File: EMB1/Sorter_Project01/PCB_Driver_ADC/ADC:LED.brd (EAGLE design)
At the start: 100 x 80 mm, 17 parts, among them IC2 LM358N, K1 612006235121, Q1 IRF512, Q2 IRF512, Q3 IRF512, Q4 IRF512

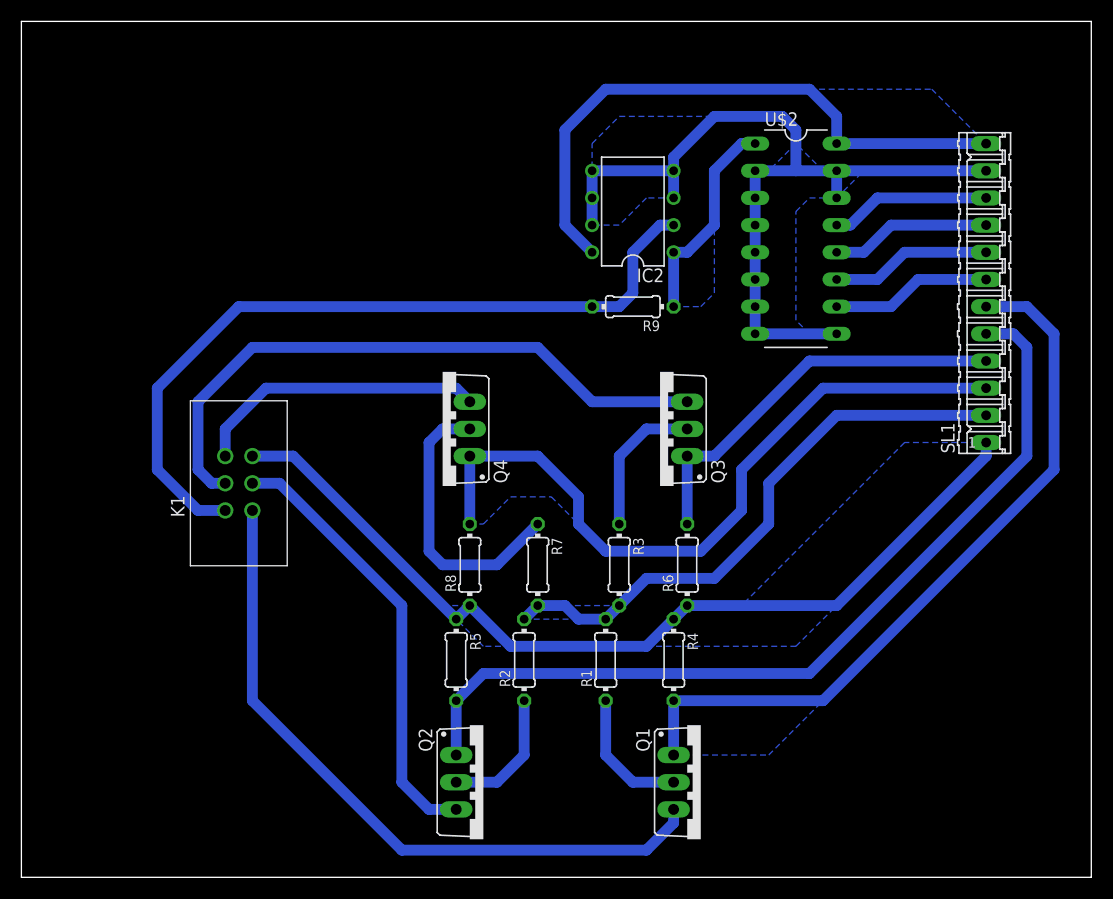
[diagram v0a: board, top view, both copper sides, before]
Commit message: Driver/ADC board modified
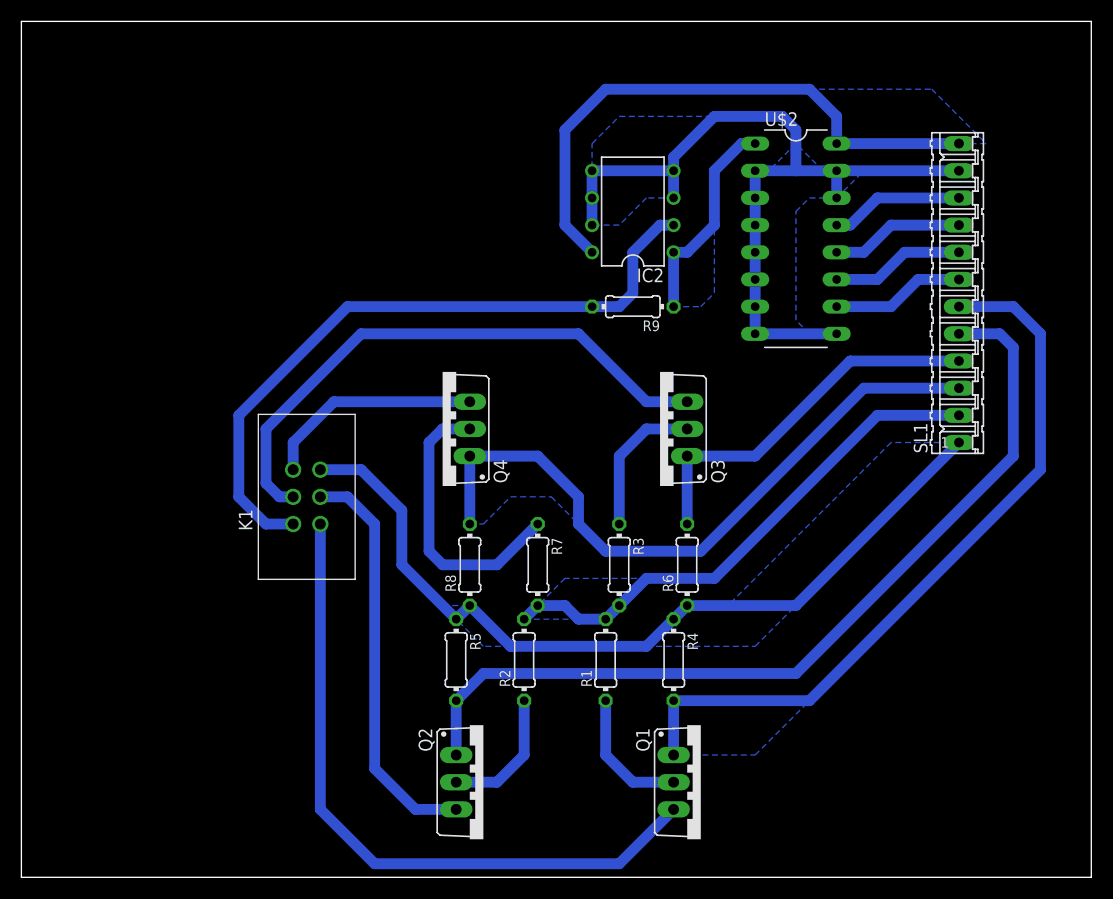
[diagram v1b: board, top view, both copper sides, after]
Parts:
- moved K1 6.48 mm to (26.7, 35.6)
- moved SL1 2.54 mm to (87.6, 54.6)
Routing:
- net GND: track 166.5 -> 156.8 mm
- net PHD: track 72.4 -> 64.0 mm
- net LED4: track 27.5 -> 20.6 mm
- net LED3: track 59.3 -> 53.8 mm
- net CTRL4: track 68.3 -> 63.6 mm
- net 12V: track 54.4 -> 49.6 mm
- net LED2: track 41.3 -> 38.2 mm
- net VDD: track 57.0 -> 54.5 mm
- net DOUT: track 15.0 -> 12.5 mm
- net DIN: track 15.0 -> 12.5 mm
- net CTRL3: track 38.0 -> 35.4 mm
- net CLK: track 15.0 -> 12.5 mm
- net *CS: track 15.0 -> 12.5 mm
- net LED1: track 65.3 -> 63.9 mm

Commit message: Printed schematic ADC/LEDS
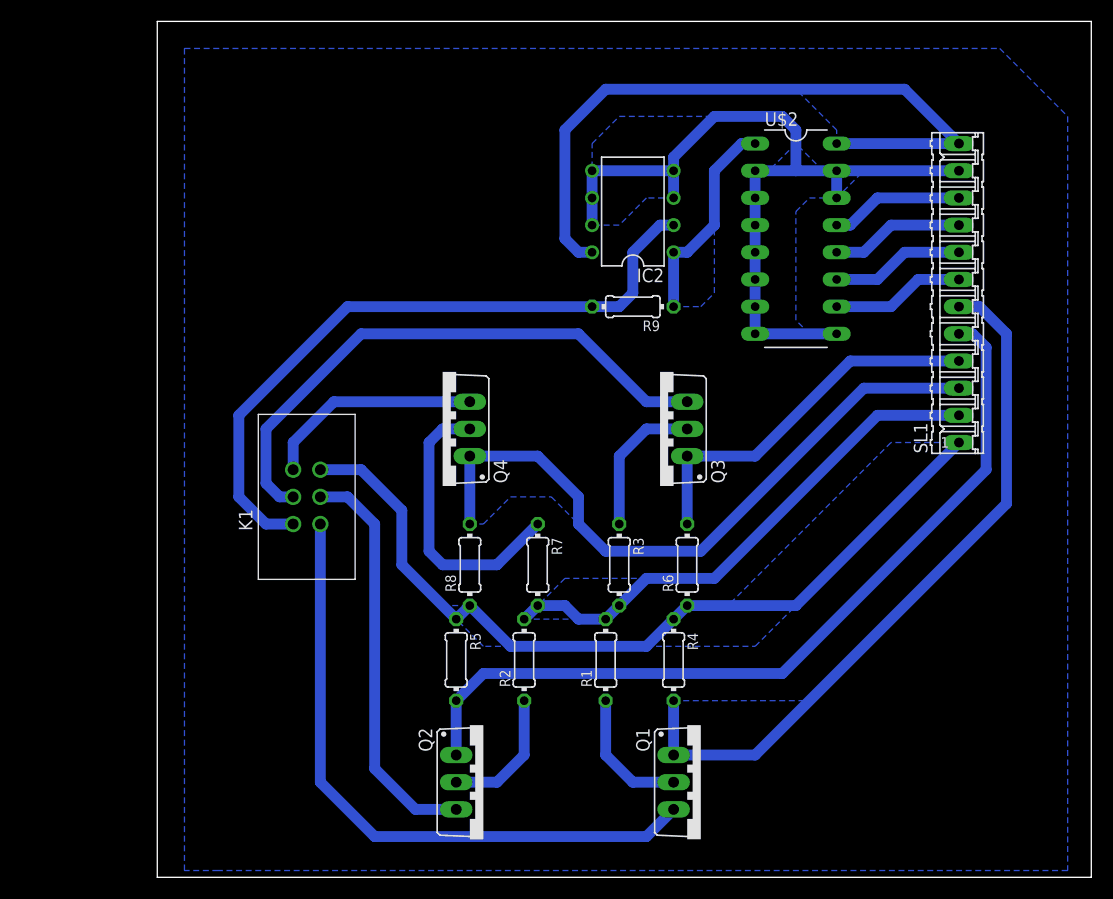
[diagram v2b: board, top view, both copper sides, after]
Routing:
- net VDD: track 54.5 -> 65.2 mm
- net CTRL2: track 82.4 -> 78.0 mm
- net LED1: track 63.9 -> 60.3 mm
- net CTRL1: track 69.7 -> 67.3 mm
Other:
- board size 100 x 80 mm -> 87.3 x 80 mm
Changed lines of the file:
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@@
 <setting verticaltext="up"/>
 </settings>
-<grid distance="0.05" unitdist="inch" unit="inch" style="lines" multiple="1" display="no" altdistance="0.025" altunitdist="inch" altunit="inch"/>
+<grid distance="0.025" unitdist="inch" unit="inch" style="lines" multiple="1" display="no" altdistance="0.025" altunitdist="inch" altunit="inch"/>
 <layers>
 <layer number="1" name="Top" color="4" fill="1" visible="yes" active="yes"/>
@@
 <layer number="17" name="Pads" color="2" fill="1" visible="yes" active="yes"/>
 <layer number="18" name="Vias" color="2" fill="1" visible="yes" active="yes"/>
-<layer number="19" name="Unrouted" color="6" fill="1" visible="yes" active="yes"/>
+<layer number="19" name="Unrouted" color="6" fill="1" visible="no" active="yes"/>
 <layer number="20" name="Dimension" color="15" fill="1" visible="yes" active="yes"/>
-<layer number="21" name="tPlace" color="7" fill="1" visible="yes" active="yes"/>
-<layer number="22" name="bPlace" color="7" fill="1" visible="yes" active="yes"/>
-<layer number="23" name="tOrigins" color="15" fill="1" visible="yes" active="yes"/>
-<layer number="24" name="bOrigins" color="15" fill="1" visible="yes" active="yes"/>
-<layer number="25" name="tNames" color="7" fill="1" visible="yes" active="yes"/>
-<layer number="26" name="bNames" color="7" fill="1" visible="yes" active="yes"/>
-<layer number="27" name="tValues" color="7" fill="1" visible="yes" active="yes"/>
-<layer number="28" name="bValues" color="7" fill="1" visible="yes" active="yes"/>
+<layer number="21" name="tPlace" color="7" fill="1" visible="no" active="yes"/>
+<layer number="22" name="bPlace" color="7" fill="1" visible="no" active="yes"/>
+<layer number="23" name="tOrigins" color="15" fill="1" visible="no" active="yes"/>
+<layer number="24" name="bOrigins" color="15" fill="1" visible="no" active="yes"/>
+<layer number="25" name="tNames" color="7" fill="1" visible="no" active="yes"/>
+<layer number="26" name="bNames" color="7" fill="1" visible="no" active="yes"/>
+<layer number="27" name="tValues" color="7" fill="1" visible="no" active="yes"/>
+<layer number="28" name="bValues" color="7" fill="1" visible="no" active="yes"/>
 <layer number="29" name="tStop" color="7" fill="3" visible="no" active="yes"/>
 <layer number="30" name="bStop" color="7" fill="6" visible="no" active="yes"/>
@@
 <layer number="37" name="tTest" color="7" fill="1" visible="no" active="yes"/>
 <layer number="38" name="bTest" color="7" fill="1" visible="no" active="yes"/>
-<layer number="39" name="tKeepout" color="4" fill="11" visible="yes" active="yes"/>
-<layer number="40" name="bKeepout" color="1" fill="11" visible="yes" active="yes"/>
-<layer number="41" name="tRestrict" color="4" fill="10" visible="yes" active="yes"/>
-<layer number="42" name="bRestrict" color="1" fill="10" visible="yes" active="yes"/>
-<layer number="43" name="vRestrict" color="2" fill="10" visible="yes" active="yes"/>
+<layer number="39" name="tKeepout" color="4" fill="11" visible="no" active="yes"/>
+<layer number="40" name="bKeepout" color="1" fill="11" visible="no" active="yes"/>
+<layer number="41" name="tRestrict" color="4" fill="10" visible="no" active="yes"/>
+<layer number="42" name="bRestrict" color="1" fill="10" visible="no" active="yes"/>
+<layer number="43" name="vRestrict" color="2" fill="10" visible="no" active="yes"/>
 <layer number="44" name="Drills" color="7" fill="1" visible="no" active="yes"/>
 <layer number="45" name="Holes" color="7" fill="1" visible="no" active="yes"/>
 <layer number="46" name="Milling" color="3" fill="1" visible="no" active="yes"/>
 <layer number="47" name="Measures" color="7" fill="1" visible="no" active="yes"/>
-<layer number="48" name="Document" color="7" fill="1" visible="yes" active="yes"/>
-<layer number="49" name="Reference" color="7" fill="1" visible="yes" active="yes"/>
-<layer number="51" name="tDocu" color="7" fill="1" visible="yes" active="yes"/>
-<layer number="52" name="bDocu" color="7" fill="1" visible="yes" active="yes"/>
+<layer number="48" name="Document" color="7" fill="1" visible="no" active="yes"/>
+<layer number="49" name="Reference" color="7" fill="1" visible="no" active="yes"/>
+<layer number="51" name="tDocu" color="7" fill="1" visible="no" active="yes"/>
+<layer number="52" name="bDocu" color="7" fill="1" visible="no" active="yes"/>
 <layer number="90" name="Modules" color="5" fill="1" visible="no" active="no"/>
 <layer number="91" name="Nets" color="2" fill="1" visible="no" active="no"/>
@@
 <board>
 <plain>
-<wire x1="0" y1="0" x2="100" y2="0" width="0" layer="20"/>
+<wire x1="12.7" y1="0" x2="100" y2="0" width="0" layer="20"/>
 <wire x1="100" y1="0" x2="100" y2="80" width="0" layer="20"/>
-<wire x1="100" y1="80" x2="0" y2="80" width="0" layer="20"/>
-<wire x1="0" y1="80" x2="0" y2="0" width="0" layer="20"/>
+<wire x1="100" y1="80" x2="12.7" y2="80" width="0" layer="20"/>
+<wire x1="12.7" y1="80" x2="12.7" y2="0" width="0" layer="20"/>
 </plain>
 <attributes>
@@
 <vertex x="62.23" y="25.4"/>
 </polygon>
+<polygon width="1.016" layer="16" isolate="1.27" thermals="no" rank="3">
+<vertex x="15.24" y="77.47"/>
+<vertex x="91.44" y="77.47"/>
+<vertex x="97.79" y="71.12"/>
+<vertex x="97.79" y="0.635"/>
+<vertex x="18.415" y="0.635"/>
+<vertex x="15.24" y="0.635"/>
+</polygon>
 <wire x1="76.2" y1="50.8" x2="87.63" y2="40.64" width="0" layer="19" extent="1-1"/>
 </signal>
@@
 <contactref element="SL1" pad="12"/>
 <wire x1="76.2" y1="68.58" x2="87.63" y2="68.58" width="1.016" layer="16"/>
-<wire x1="76.2" y1="68.58" x2="76.2" y2="71.12" width="1.016" layer="16"/>
-<wire x1="76.2" y1="71.12" x2="73.66" y2="73.66" width="1.016" layer="16"/>
-<wire x1="73.66" y1="73.66" x2="54.61" y2="73.66" width="1.016" layer="16"/>
-<wire x1="54.61" y1="73.66" x2="50.8" y2="69.85" width="1.016" layer="16"/>
-<wire x1="50.8" y1="69.85" x2="50.8" y2="60.96" width="1.016" layer="16"/>
-<wire x1="50.8" y1="60.96" x2="53.34" y2="58.42" width="1.016" layer="16"/>
-<polygon width="1.016" layer="16" thermals="no">
-<vertex x="73.66" y="73.66"/>
-<vertex x="85.09" y="73.66"/>
-<vertex x="90.17" y="68.58"/>
+<wire x1="53.34" y1="58.42" x2="52.07" y2="58.42" width="1.016" layer="16"/>
+<wire x1="52.07" y1="58.42" x2="50.8" y2="59.69" width="1.016" layer="16"/>
+<wire x1="50.8" y1="59.69" x2="50.8" y2="69.85" width="1.016" layer="16"/>
+<wire x1="50.8" y1="69.85" x2="54.61" y2="73.66" width="1.016" layer="16"/>
+<wire x1="54.61" y1="73.66" x2="82.55" y2="73.66" width="1.016" layer="16"/>
+<wire x1="82.55" y1="73.66" x2="87.63" y2="68.58" width="1.016" layer="16"/>
+<polygon width="1.016" layer="16" thermals="no">
 <vertex x="76.2" y="68.58"/>
-<vertex x="76.2" y="71.12"/>
+<vertex x="76.2" y="69.85"/>
+<vertex x="72.39" y="73.66"/>
+<vertex x="82.55" y="73.66"/>
+<vertex x="87.63" y="68.58"/>
 </polygon>
 </signal>
@@
 <wire x1="40.64" y1="16.51" x2="40.64" y2="11.43" width="1.016" layer="16"/>
 <wire x1="40.64" y1="16.51" x2="43.18" y2="19.05" width="1.016" layer="16"/>
-<wire x1="43.18" y1="19.05" x2="72.39" y2="19.05" width="1.016" layer="16"/>
-<wire x1="72.39" y1="19.05" x2="92.71" y2="39.37" width="1.016" layer="16"/>
-<wire x1="92.71" y1="39.37" x2="92.71" y2="49.53" width="1.016" layer="16"/>
-<wire x1="92.71" y1="49.53" x2="91.44" y2="50.8" width="1.016" layer="16"/>
-<wire x1="91.44" y1="50.8" x2="87.63" y2="50.8" width="1.016" layer="16"/>
+<wire x1="43.18" y1="19.05" x2="71.12" y2="19.05" width="1.016" layer="16"/>
+<wire x1="71.12" y1="19.05" x2="90.17" y2="38.1" width="1.016" layer="16"/>
+<wire x1="90.17" y1="38.1" x2="90.17" y2="49.53" width="1.016" layer="16"/>
+<wire x1="90.17" y1="49.53" x2="88.9" y2="50.8" width="1.016" layer="16"/>
+<wire x1="88.9" y1="50.8" x2="87.63" y2="50.8" width="1.016" layer="16"/>
 </signal>
 <signal name="CTRL3">
@@
 <contactref element="Q1" pad="G"/>
 <contactref element="SL1" pad="6"/>
+<wire x1="87.63" y1="53.34" x2="89.535" y2="53.34" width="1.016" layer="16"/>
+<wire x1="89.535" y1="53.34" x2="92.075" y2="50.8" width="1.016" layer="16"/>
+<wire x1="92.075" y1="50.8" x2="92.075" y2="34.925" width="1.016" layer="16"/>
+<wire x1="92.075" y1="34.925" x2="68.58" y2="11.43" width="1.016" layer="16"/>
+<wire x1="60.96" y1="11.43" x2="68.58" y2="11.43" width="1.016" layer="16"/>
 <wire x1="60.96" y1="16.51" x2="60.96" y2="11.43" width="1.016" layer="16"/>
-<wire x1="87.63" y1="53.34" x2="92.71" y2="53.34" width="1.016" layer="16"/>
-<wire x1="92.71" y1="53.34" x2="95.25" y2="50.8" width="1.016" layer="16"/>
-<wire x1="95.25" y1="50.8" x2="95.25" y2="38.1" width="1.016" layer="16"/>
-<wire x1="95.25" y1="38.1" x2="73.66" y2="16.51" width="1.016" layer="16"/>
-<wire x1="73.66" y1="16.51" x2="60.96" y2="16.51" width="1.016" layer="16"/>
-<polygon width="1.016" layer="16" thermals="no">
+<polygon width="1.016" layer="16" thermals="no">
+<vertex x="60.96" y="16.51"/>
+<vertex x="73.66" y="16.51"/>
+<vertex x="68.58" y="11.43"/>
 <vertex x="60.96" y="11.43"/>
-<vertex x="68.58" y="11.43"/>
-<vertex x="73.66" y="16.51"/>
-<vertex x="60.96" y="16.51"/>
 </polygon>
 </signal>
@@
 <contactref element="K1" pad="1"/>
 <contactref element="Q1" pad="S"/>
-<wire x1="27.94" y1="33.02" x2="27.94" y2="6.35" width="1.016" layer="16"/>
-<wire x1="27.94" y1="6.35" x2="33.02" y2="1.27" width="1.016" layer="16"/>
-<wire x1="33.02" y1="1.27" x2="55.88" y2="1.27" width="1.016" layer="16"/>
-<wire x1="55.88" y1="1.27" x2="60.96" y2="6.35" width="1.016" layer="16"/>
+<wire x1="27.94" y1="33.02" x2="27.94" y2="8.89" width="1.016" layer="16"/>
+<wire x1="27.94" y1="8.89" x2="33.02" y2="3.81" width="1.016" layer="16"/>
+<wire x1="33.02" y1="3.81" x2="58.42" y2="3.81" width="1.016" layer="16"/>
+<wire x1="58.42" y1="3.81" x2="60.96" y2="6.35" width="1.016" layer="16"/>
 </signal>
 <signal name="LED2">
